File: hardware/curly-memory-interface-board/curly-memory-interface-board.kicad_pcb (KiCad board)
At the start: 2 copper layers, 30 x 100.5 mm, 27 parts, among them J1 AudioJack2, J10 AudioJack2, J101 Conn_01x05, J11 AudioJack2, J12 Conn_01x05, J13 Conn_01x05, J14 Conn_01x05, J15 Conn_01x05, J16 Conn_01x05, J17 PinSocket_1x02_P2.54mm_Vertic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, J2 AudioJack2, J3 AudioJack2, J5 Conn_01x05, J6 Conn_01x05, J7 Conn_01x05, J8 AudioJack2, J9 AudioJack2, SW1 FSM, SW2 FSM, SW3 FSM, SW4 FSM

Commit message: all components placed on the main board
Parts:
- removed J101: Conn_01x05, Connector_PinSocket_2.54mm:PinSocket_1x11_P2.54mm_Vertical
- added J4: Conn_01x11, Connector_PinSocket_2.54mm:PinSocket_1x11_P2.54mm_Vertical, B.Cu at (2.30, 31.6)
- J12, J13, J15, J16: footprint Connector_PinSocket_2.54mm:PinSocket_1x05_P2.54mm_Vertical -> Connector_PinHeader_2.54mm:PinHeader_1x05_P2.54mm_Vertical
- J17: value PinSocket_1x02_P2.54mm_Vertical -> Conn_01x02
- moved J14 2.63 mm to (17.5, 71.3)
- moved J6 2.43 mm to (2.30, 71.5)
- moved J12 2.07 mm to (2.30, 68.9)
- moved J16 2.07 mm to (17.5, 68.9)
- moved D1 1.73 mm to (7.54, 64.0)
- moved J15 1.69 mm to (17.5, 75.2)
- moved J17 1.57 mm to (15.0, 62.8)
- moved J13 1.30 mm to (2.30, 75.2)
- moved D2 1.29 mm to (22.4, 64.0)
- moved J5 0.49 mm to (17.5, 79.2)
- moved J10 0.37 mm to (7.37, 94.9)
- moved J11 0.37 mm to (22.2, 94.9)
- moved J8 0.37 mm to (7.37, 84.8)
- moved J9 0.37 mm to (22.2, 84.8)
- moved J7 0.17 mm to (2.30, 79.2)
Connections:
- D1 pad 2: Net-(D102-Pad2) -> Net-(D1-Pad2)
- D1 pad 4: Net-(D101-Pad2) -> /LEDS
- D2 pad 2: Net-(D102-Pad2) -> unconnected-(D2-Pad2)
- D2 pad 4: Net-(D101-Pad2) -> Net-(D1-Pad2)
- J1 pad S: Net-(J201-PadS) -> GND
- J1 pad T: GND -> /IN_0
- J1 pad TN: GND -> /IN_0
- J10 pad S: /output/OUT_1 -> GND
- J10 pad T: GND -> /OUT_2
- J10 pad TN: GND -> /OUT_2
- J11 pad S: /output/OUT_2 -> /DryWet
- J12 pad 1: (no net) -> /BOOT
- J12 pad 2: (no net) -> /RST
- J12 pad 3: (no net) -> /PROG_TX
- J12 pad 4: (no net) -> /PROG_RX
- J12 pad 5: (no net) -> GND
- J13 pad 1: (no net) -> /RES0_A1
- J13 pad 2: (no net) -> /RES0_W1
- J13 pad 3: (no net) -> /RES0_B1
- J13 pad 4: (no net) -> /LEDS
- J13 pad 5: (no net) -> GND
- J14 pad 1: (no net) -> /IO17
- J14 pad 2: (no net) -> /IO21
- J14 pad 3: (no net) -> /IO22
- J14 pad 4: (no net) -> +3V3
- J14 pad 5: (no net) -> +5V
- J15 pad 1: (no net) -> /IN_3
- J15 pad 2: (no net) -> /OUT_3
- J15 pad 3: (no net) -> /IN_2
- J15 pad 4: (no net) -> /OUT_2
- J15 pad 5: (no net) -> GND
- J16 pad 1: (no net) -> /IO17
- J16 pad 2: (no net) -> /IO21
- J16 pad 3: (no net) -> /IO22
- J16 pad 4: (no net) -> +3V3
- J16 pad 5: (no net) -> +5V
- J17 pad 1: (no net) -> unconnected-(J17-Pad1)
- J17 pad 2: (no net) -> unconnected-(J17-Pad2)
- J2 pad S: Net-(J202-PadS) -> GND
- J2 pad T: GND -> /IN_1
- J2 pad TN: GND -> /IN_1
- J3 pad S: Net-(J203-PadS) -> GND
- J3 pad T: GND -> /IN_2
- J3 pad TN: GND -> /IN_2
- J5 pad 1: (no net) -> /DryWet
- J5 pad 2: (no net) -> /OUT_3
- J5 pad 3: (no net) -> /OUT_2
- J5 pad 4: (no net) -> /OUT_1
- J5 pad 5: (no net) -> /OUT_0
- J6 pad 1: (no net) -> /BOOT
- J6 pad 2: (no net) -> /RST
- J6 pad 3: (no net) -> /PROG_TX
- J6 pad 4: (no net) -> /PROG_RX
- J6 pad 5: (no net) -> GND
- J7 pad 1: (no net) -> /RES0_A1
- J7 pad 2: (no net) -> /RES0_W1
- J7 pad 3: (no net) -> /RES0_B1
- J7 pad 4: (no net) -> /LEDS
- J7 pad 5: (no net) -> GND
- J8 pad S: /output/OUT_3 -> GND
- J8 pad T: GND -> /OUT_0
- J8 pad TN: GND -> /OUT_0
- J9 pad S: /output/OUT_0 -> GND
- J9 pad T: GND -> /OUT_1
- J9 pad TN: GND -> /OUT_1
- RV1 pad 2: /RES_2 -> /RES_0
- RV2 pad 2: /RES_0 -> /RES_1
- RV3 pad 2: /RES_3 -> /RES_2
- RV4 pad 2: /RES_1 -> /RES_3
- SW1 pad 1: /SW_1 -> /SW_0
- SW1 pad 2: /SW_1 -> /SW_0
- SW2 pad 1: GND -> /SW_1
- SW2 pad 2: GND -> /SW_1
- SW3 pad 1: /SW_0 -> /RST
- SW3 pad 2: /SW_0 -> /RST
- SW4 pad 1: GND -> /BOOT
- SW4 pad 2: GND -> /BOOT
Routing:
- added copper zone on B.Cu, net GND
- added copper zone on F.Cu, net GND
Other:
- board size 30 x 100.5 mm -> 30 x 100 mm

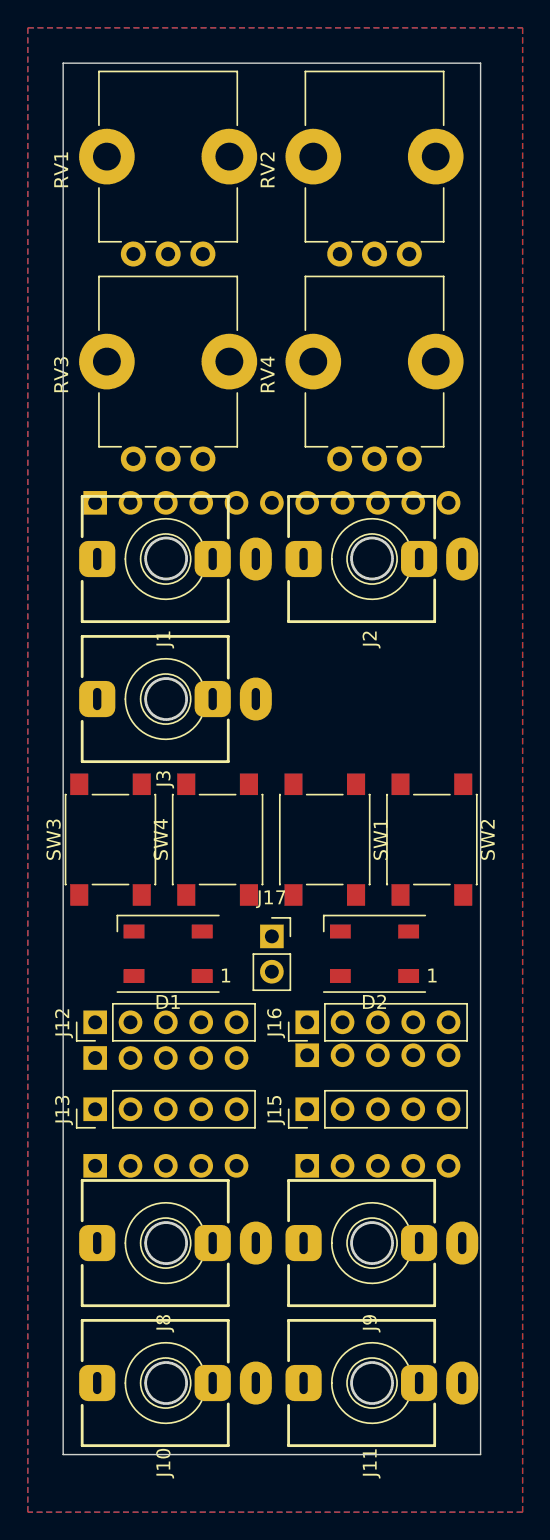
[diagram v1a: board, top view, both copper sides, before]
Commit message: more pcb tracked
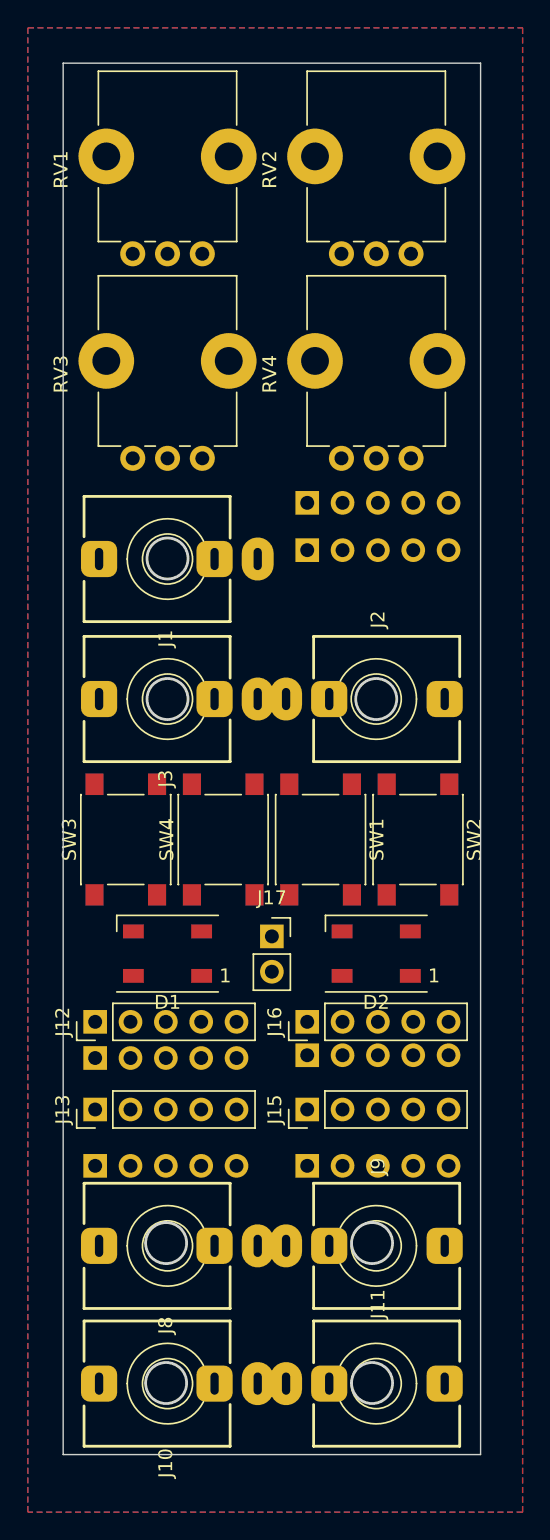
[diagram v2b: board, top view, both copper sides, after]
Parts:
- added J18: Conn_01x05, Connector_PinSocket_2.54mm:PinSocket_1x05_P2.54mm_Vertical, B.Cu at (17.5, 35.0)
- J4: value Conn_01x11 -> Conn_01x05; footprint Connector_PinSocket_2.54mm:PinSocket_1x11_P2.54mm_Vertical -> Connector_PinSocket_2.54mm:PinSocket_1x05_P2.54mm_Vertical
- moved J4 15.2 mm to (17.5, 31.6)
- moved J2 10.1 mm to (22.5, 45.7), turned to -90 degrees
- moved SW3 1.10 mm to (4.50, 55.8)
- moved SW2 1.00 mm to (25.5, 55.8)
- moved SW4 0.40 mm to (11.5, 55.8)
- moved J9 0.36 mm to (22.5, 85.0), turned to -90 degrees
- moved J11 0.30 mm to (22.5, 94.9), turned to -90 degrees
- moved SW1 0.30 mm to (18.5, 55.8)
- moved J8 0.24 mm to (7.50, 85.0)
- moved J10 0.14 mm to (7.50, 94.9)
- moved J1 0.13 mm to (7.50, 35.6)
- moved J3 0.13 mm to (7.50, 45.7)
- moved RV4 0.13 mm to (25.0, 28.4)
- moved RV2 0.12 mm to (25.0, 13.7)
- moved D2 0.12 mm to (22.5, 64.0)
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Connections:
- J1 pad TN: /IN_0 -> GND
- J10 pad TN: /OUT_2 -> GND
- J11 pad S: /DryWet -> GND
- J11 pad T: GND -> /DryWet
- J2 pad TN: /IN_1 -> GND
- J3 pad TN: /IN_2 -> GND
- J8 pad TN: /OUT_0 -> GND
- J9 pad TN: /OUT_1 -> GND
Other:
- outline, holes or cut-outs redrawn

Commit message: interface board tracked and silkscreen sorted
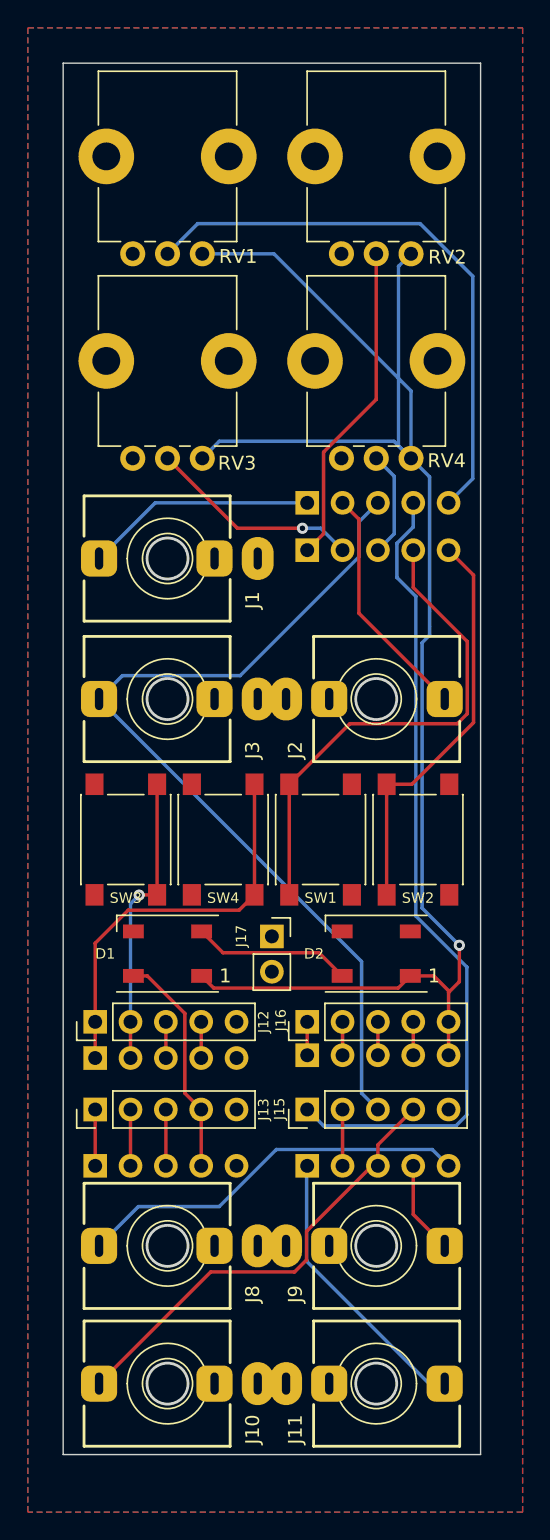
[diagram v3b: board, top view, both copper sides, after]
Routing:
- net +5V: track 0.00 -> 119.5 mm, vias 0 -> 1
- net /IN_2: track 0.00 -> 65.2 mm
- net /IN_3: track 0.00 -> 58.8 mm
- net /RES_0: track 0.00 -> 41.4 mm
- net /SW_0: track 0.00 -> 36.2 mm
- net /OUT_2: track 0.00 -> 32.8 mm
- net /SW_1: track 0.00 -> 29.2 mm
- net /BOOT: track 0.00 -> 29.1 mm
- net /OUT_0: track 0.00 -> 28.5 mm
- net /RES_1: track 0.00 -> 23.4 mm
- net /RST: track 0.00 -> 21.2 mm, vias 0 -> 1
- net /DryWet: track 0.00 -> 20.4 mm
- net /IN_1: track 0.00 -> 17.1 mm
- net /IN_0: track 0.00 -> 16.6 mm
- net /LEDS: track 0.00 -> 16.3 mm
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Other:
- outline, holes or cut-outs redrawn
- board text added: "rfe"
- board text added: "ric from ealing curly memory interface board issue A"

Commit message: all hardware finished
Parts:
- renumbered J3 to J2, J2 to J3
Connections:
- net /IO22 renamed /V_OFFSET
- J14 pad 1: /IO17 -> +5V
- J14 pad 2: /IO21 -> +3V3
- J14 pad 4: +3V3 -> /IO_32
- J14 pad 5: +5V -> /IO_21
- J16 pad 1: /IO17 -> +5V
- J16 pad 2: /IO21 -> +3V3
- J16 pad 4: +3V3 -> /IO_32
- J16 pad 5: +5V -> /IO_21
- J2 pad T: /IN_2 -> /IN_1
- J3 pad T: /IN_1 -> /IN_2
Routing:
- net /IN_2: track 65.2 -> 51.1 mm, vias 0 -> 2
- net /IN_1: track 17.1 -> 28.5 mm
- net /IO_32: track 0.00 -> 2.40 mm
- net /IO_21: track 0.00 -> 2.40 mm
- net /IO21: track 2.40 -> 0.00 mm
- net /IO17: track 2.40 -> 0.00 mm
- net +5V: track 119.5 -> 117.3 mm, vias 1 -> 2

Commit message: gerbers genearted and mf/mfpn added for main board for build
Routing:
- net /RES_1: track 23.4 -> 24.3 mm
- net GND: vias 0 -> 50
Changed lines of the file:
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@@
       (plotinvisibletext false)
       (sketchpadsonfab false)
-      (subtractmaskfromsilk false)
+      (subtractmaskfromsilk true)
       (outputformat 1)
       (mirror false)
-      (drillshape 1)
+      (drillshape 0)
       (scaleselection 1)
-      (outputdirectory "")
+      (outputdirectory "cm-interface-gerbers")
     )
   )
@@
   (segment (start 4.84 68.9) (end 4.84 66.0794) (width 0.25) (layer "B.Cu") (net 1))
   (segment (start 4.84 66.0794) (end 4.84 60.4126) (width 0.25) (layer "B.Cu") (net 1))
+  (via (at 11.176 77.47) (size 0.8) (drill 0.4) (layers "F.Cu" "B.Cu") (free) (net 2))
+  (via (at 6.096 73.406) (size 0.8) (drill 0.4) (layers "F.Cu" "B.Cu") (free) (net 2))
+  (via (at 21.59 25.4) (size 0.8) (drill 0.4) (layers "F.Cu" "B.Cu") (free) (net 2))
+  (via (at 3.556 77.47) (size 0.8) (drill 0.4) (layers "F.Cu" "B.Cu") (free) (net 2))
+  (via (at 11.176 73.406) (size 0.8) (drill 0.4) (layers "F.Cu" "B.Cu") (free) (net 2))
+  (via (at 6.35 25.4) (size 0.8) (drill 0.4) (layers "F.Cu" "B.Cu") (free) (net 2))
+  (via (at 18.796 73.152) (size 0.8) (drill 0.4) (layers "F.Cu" "B.Cu") (free) (net 2))
+  (via (at 26.416 70.104) (size 0.8) (drill 0.4) (layers "F.Cu" "B.Cu") (free) (net 2))
+  (via (at 8.89 25.4) (size 0.8) (drill 0.4) (layers "F.Cu" "B.Cu") (free) (net 2))
+  (via (at 22.86 6.35) (size 0.8) (drill 0.4) (layers "F.Cu" "B.Cu") (free) (net 2))
+  (via (at 24.13 10.16) (size 0.8) (drill 0.4) (layers "F.Cu" "B.Cu") (free) (net 2))
+  (via (at 26.416 73.152) (size 0.8) (drill 0.4) (layers "F.Cu" "B.Cu") (free) (net 2))
+  (via (at 24.13 77.216) (size 0.8) (drill 0.4) (layers "F.Cu" "B.Cu") (free) (net 2))
+  (via (at 21.59 77.216) (size 0.8) (drill 0.4) (layers "F.Cu" "B.Cu") (free) (net 2))
+  (via (at 3.81 70.358) (size 0.8) (drill 0.4) (layers "F.Cu" "B.Cu") (free) (net 2))
+  (via (at 8.636 77.47) (size 0.8) (drill 0.4) (layers "F.Cu" "B.Cu") (free) (net 2))
+  (via (at 8.89 10.16) (size 0.8) (drill 0.4) (layers "F.Cu" "B.Cu") (free) (net 2))
+  (via (at 7.62 21.59) (size 0.8) (drill 0.4) (layers "F.Cu" "B.Cu") (free) (net 2))
+  (via (at 7.62 6.35) (size 0.8) (drill 0.4) (layers "F.Cu" "B.Cu") (free) (net 2))
+  (via (at 24.13 2.54) (size 0.8) (drill 0.4) (layers "F.Cu" "B.Cu") (free) (net 2))
+  (via (at 26.67 77.216) (size 0.8) (drill 0.4) (layers "F.Cu" "B.Cu") (free) (net 2))
+  (via (at 11.43 57.15) (size 0.8) (drill 0.4) (layers "F.Cu" "B.Cu") (free) (net 2))
+  (via (at 21.59 2.54) (size 0.8) (drill 0.4) (layers "F.Cu" "B.Cu") (free) (net 2))
+  (via (at 3.81 57.15) (size 0.8) (drill 0.4) (layers "F.Cu" "B.Cu") (free) (net 2))
+  (via (at 22.86 40.64) (size 0.8) (drill 0.4) (layers "F.Cu" "B.Cu") (free) (net 2))
+  (via (at 6.35 10.16) (size 0.8) (drill 0.4) (layers "F.Cu" "B.Cu") (free) (net 2))
+  (via (at 6.35 2.54) (size 0.8) (drill 0.4) (layers "F.Cu" "B.Cu") (free) (net 2))
+  (via (at 8.89 2.54) (size 0.8) (drill 0.4) (layers "F.Cu" "B.Cu") (free) (net 2))
+  (via (at 17.78 57.15) (size 0.8) (drill 0.4) (layers "F.Cu" "B.Cu") (free) (net 2))
+  (via (at 3.556 73.406) (size 0.8) (drill 0.4) (layers "F.Cu" "B.Cu") (free) (net 2))
+  (via (at 21.59 17.78) (size 0.8) (drill 0.4) (layers "F.Cu" "B.Cu") (free) (net 2))
+  (via (at 19.05 77.216) (size 0.8) (drill 0.4) (layers "F.Cu" "B.Cu") (free) (net 2))
+  (via (at 11.176 70.358) (size 0.8) (drill 0.4) (layers "F.Cu" "B.Cu") (free) (net 2))
+  (via (at 7.62 40.64) (size 0.8) (drill 0.4) (layers "F.Cu" "B.Cu") (free) (net 2))
+  (via (at 6.096 70.358) (size 0.8) (drill 0.4) (layers "F.Cu" "B.Cu") (free) (net 2))
+  (via (at 22.86 62.23) (size 0.8) (drill 0.4) (layers "F.Cu" "B.Cu") (free) (net 2))
+  (via (at 7.62 62.23) (size 0.8) (drill 0.4) (layers "F.Cu" "B.Cu") (free) (net 2))
+  (via (at 3.81 54.61) (size 0.8) (drill 0.4) (layers "F.Cu" "B.Cu") (free) (net 2))
+  (via (at 8.89 17.78) (size 0.8) (drill 0.4) (layers "F.Cu" "B.Cu") (free) (net 2))
+  (via (at 21.59 57.15) (size 0.8) (drill 0.4) (layers "F.Cu" "B.Cu") (free) (net 2))
+  (via (at 23.876 70.104) (size 0.8) (drill 0.4) (layers "F.Cu" "B.Cu") (free) (net 2))
+  (via (at 15.24 2.54) (size 0.8) (drill 0.4) (layers "F.Cu" "B.Cu") (free) (net 2))
+  (via (at 23.876 73.152) (size 0.8) (drill 0.4) (layers "F.Cu" "B.Cu") (free) (net 2))
+  (via (at 21.59 54.61) (size 0.8) (drill 0.4) (layers "F.Cu" "B.Cu") (free) (net 2))
+  (via (at 15.24 10.16) (size 0.8) (drill 0.4) (layers "F.Cu" "B.Cu") (free) (net 2))
+  (via (at 11.43 54.61) (size 0.8) (drill 0.4) (layers "F.Cu" "B.Cu") (free) (net 2))
+  (via (at 6.096 77.47) (size 0.8) (drill 0.4) (layers "F.Cu" "B.Cu") (free) (net 2))
+  (via (at 17.78 54.61) (size 0.8) (drill 0.4) (layers "F.Cu" "B.Cu") (free) (net 2))
+  (via (at 21.59 10.16) (size 0.8) (drill 0.4) (layers "F.Cu" "B.Cu") (free) (net 2))
+  (via (at 6.35 17.78) (size 0.8) (drill 0.4) (layers "F.Cu" "B.Cu") (free) (net 2))
   (segment (start 9.95 65.6) (end 10.822511 66.472511) (width 0.25) (layer "F.Cu") (net 3))
   (segment (start 29.21 31.44899) (end 26.16101 28.4) (width 0.25) (layer "F.Cu") (net 3))
@@
   (segment (start 20.08 79.25) (end 20.08 75.2) (width 0.25) (layer "F.Cu") (net 9))
   (segment (start 10.60548 86.87452) (end 2.58 94.9) (width 0.25) (layer "F.Cu") (net 10))
-  (segment (start 22.62 77.74) (end 25.16 75.2) (width 0.25) (layer "F.Cu") (net 10))
+  (segment (start 22.62 77.456) (end 24.876 75.2) (width 0.25) (layer "F.Cu") (net 10))
+  (segment (start 22.62 79.25) (end 22.62 77.456) (width 0.25) (layer "F.Cu") (net 10))
   (segment (start 22.62 79.25) (end 22.191821 79.25) (width 0.25) (layer "F.Cu") (net 10))
   (segment (start 22.191821 79.25) (end 17.49548 83.946341) (width 0.25) (layer "F.Cu") (net 10))
   (segment (start 17.49548 86.009806) (end 16.630766 86.87452) (width 0.25) (layer "F.Cu") (net 10))
-  (segment (start 22.62 79.25) (end 22.62 77.74) (width 0.25) (layer "F.Cu") (net 10))
+  (segment (start 24.876 75.2) (end 25.16 75.2) (width 0.25) (layer "F.Cu") (net 10))
   (segment (start 17.49548 83.946341) (end 17.49548 86.009806) (width 0.25) (layer "F.Cu") (net 10))
   (segment (start 16.630766 86.87452) (end 10.60548 86.87452) (width 0.25) (layer "F.Cu") (net 10))
@@
   (segment (start 25.654 11.5316) (end 9.6684 11.5316) (width 0.25) (layer "B.Cu") (net 30))
   (segment (start 27.7 31.6) (end 29.4386 29.8614) (width 0.25) (layer "B.Cu") (net 30))
+  (segment (start 19.49279 27.175489) (end 18.714511 27.953768) (width 0.25) (layer "F.Cu") (net 31))
   (segment (start 18.714511 27.953768) (end 18.714511 33.825489) (width 0.25) (layer "F.Cu") (net 31))
-  (segment (start 22.5 24.168279) (end 18.714511 27.953768) (width 0.25) (layer "F.Cu") (net 31))
+  (segment (start 22.5 13.7) (end 22.5 25.76) (width 0.25) (layer "F.Cu") (net 31))
+  (segment (start 21.084511 27.175489) (end 19.49279 27.175489) (width 0.25) (layer "F.Cu") (net 31))
+  (segment (start 22.5 25.76) (end 21.084511 27.175489) (width 0.25) (layer "F.Cu") (net 31))
   (segment (start 18.714511 33.825489) (end 17.54 35) (width 0.25) (layer "F.Cu") (net 31))
-  (segment (start 22.5 13.7) (end 22.5 24.168279) (width 0.25) (layer "F.Cu") (net 31))
   (segment (start 12.5264 33.4264) (end 7.5 28.4) (width 0.25) (layer "F.Cu") (net 32))
   (segment (start 17.1958 33.4264) (end 12.5264 33.4264) (width 0.25) (layer "F.Cu") (net 32))
